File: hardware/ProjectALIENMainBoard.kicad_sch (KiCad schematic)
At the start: 53 parts, among them J1 Bumper, J10 Excess GPIO Pins, J3 Left Motor, J4 Right Motor, J5 Pixels, J6 Ultrasonic, J7 Micro USB, J8 I2C Multiplexer, J9 Voltage Breakout, Q1 2N3904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

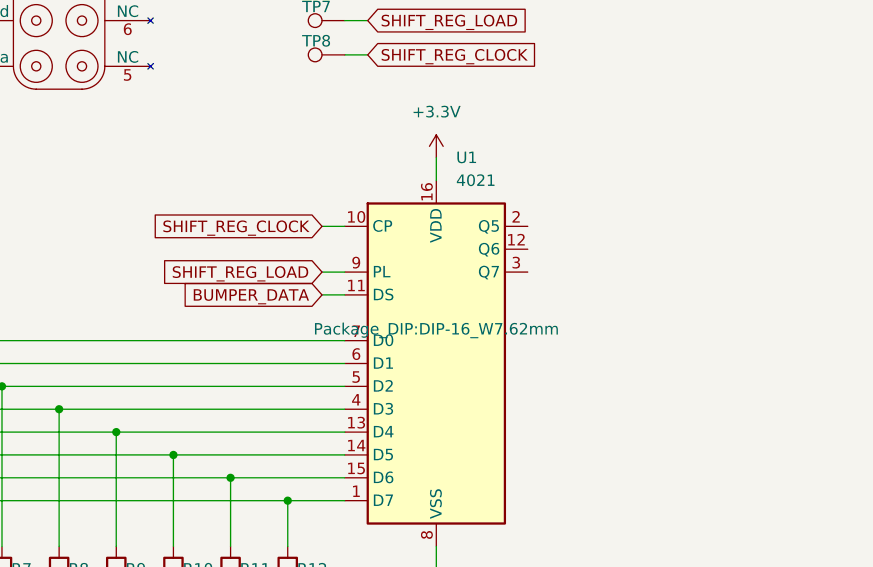
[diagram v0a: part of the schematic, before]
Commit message: Fixed direction of connectors
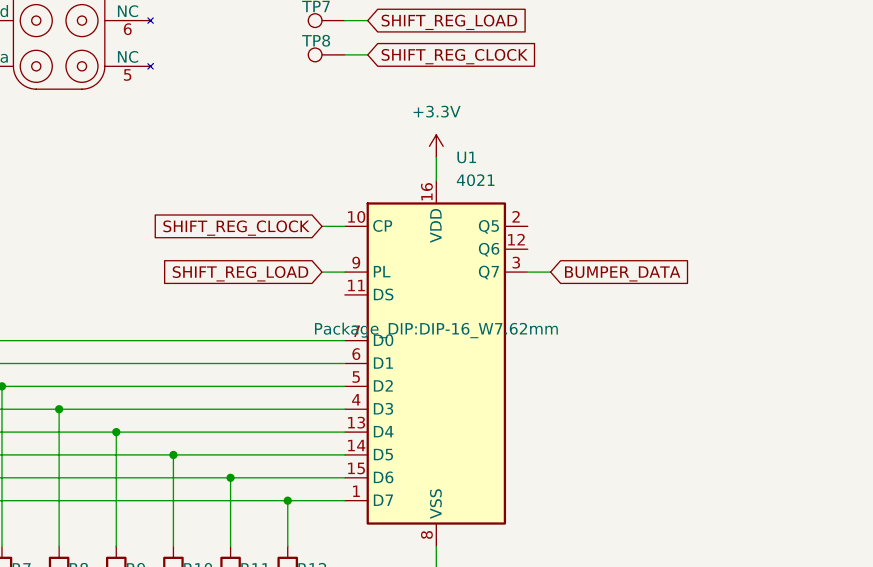
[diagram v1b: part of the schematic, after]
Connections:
- net BUMPER_DATA: now also U1.3 (Q7); no longer U1.11 (DS)
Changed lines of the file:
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@@
+	(wire
+		(pts
+			(xy 111.76 110.49) (xy 114.3 110.49)
+		)
+		(stroke
+			(width 0)
+			(type default)
+		)
+	)
 	(wire
 		(pts
@@
 		(pts
 			(xy 78.74 133.35) (xy 91.44 133.35)
-		)
-		(stroke
-			(width 0)
-			(type default)
-		)
-	)
-	(wire
-		(pts
-			(xy 88.9 113.03) (xy 91.44 113.03)
 		)
 		(stroke
@@
 		)
 	)
+	(global_label "BUMPER_DATA"
+		(shape input)
+		(at 114.3 110.49 0)
+		(fields_autoplaced yes)
+		(effects
+			(font
+				(size 1.27 1.27)
+			)
+			(justify left)
+		)
+		(property "Intersheetrefs" "${INTERSHEET_REFS}"
+			(at 130.4085 110.49 0)
+			(effects
+				(font
+					(size 1.27 1.27)
+				)
+				(justify left)
+				(hide yes)
+			)
+		)
+	)
 	(global_label "ENC1B"
 		(shape input)
@@
 			(effects
 				(font
-					(size 1.27 1.27)
-				)
-				(justify right)
-				(hide yes)
-			)
-		)
-	)
-	(global_label "BUMPER_DATA"
-		(shape input)
-		(at 88.9 113.03 180)
-		(fields_autoplaced yes)
-		(effects
-			(font
-				(size 1.27 1.27)
-			)
-			(justify right)
-		)
-		(property "Intersheetrefs" "${INTERSHEET_REFS}"
-			(at 72.7915 113.03 0)
-			(effects
-				(font

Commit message: Updated designators
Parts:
- renumbered A1 to U1, M1 to U2, U1 to U3
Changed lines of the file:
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@@
 		(dnp no)
 		(fields_autoplaced yes)
-		(property "Reference" "U1"
+		(property "Reference" "U3"
+			(at 103.7941 95.25 0)
+			(effects
+				(font
+					(size 1.27 1.27)
+				)
+				(justify left)
+			)
+		)
+		(property "Value" "4021"
 			(at 103.7941 97.79 0)
 			(effects
@@
 			)
 		)
-		(property "Value" "4021"
+		(property "Footprint" "Package_DIP:DIP-16_W7.62mm"
 			(at 103.7941 100.33 0)
 			(effects
@@
 				)
 				(justify left)
-			)
-		)
-		(property "Footprint" "Package_DIP:DIP-16_W7.62mm"
-			(at 101.6 116.84 0)
-			(effects
-				(font
-					(size 1.27 1.27)
-				)
 			)
 		)
@@
 			(project "ProjectALIENMainBoard"
 				(path "/170b00d5-17da-40d3-a37d-b29c3db0afc1"
-					(reference "U1")
+					(reference "U3")
 					(unit 1)
 				)
@@
 		(on_board yes)
 		(dnp no)
-		(property "Reference" "M1"
+		(property "Reference" "U2"
 			(at 152.4 44.45 0)
 			(effects
@@
 			(project "ProjectALIENMainBoard"
 				(path "/170b00d5-17da-40d3-a37d-b29c3db0afc1"
-					(reference "M1")
+					(reference "U2")
 					(unit 1)
 				)
@@
 		(on_board yes)
 		(dnp no)
-		(property "Reference" "A1"
+		(property "Reference" "U1"
 			(at 265.7759 154.94 0)
 			(effects
@@
 			(project "ProjectALIENMainBoard"
 				(path "/170b00d5-17da-40d3-a37d-b29c3db0afc1"
-					(reference "A1")
-					(unit 1)
-				)
+					(reference "U1")
+					(unit 1)
+				)
